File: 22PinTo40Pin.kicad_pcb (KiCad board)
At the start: 2 copper layers, 92 x 15 mm, 3 parts, among them J1 Conn_01x15, J2 Conn_01x22

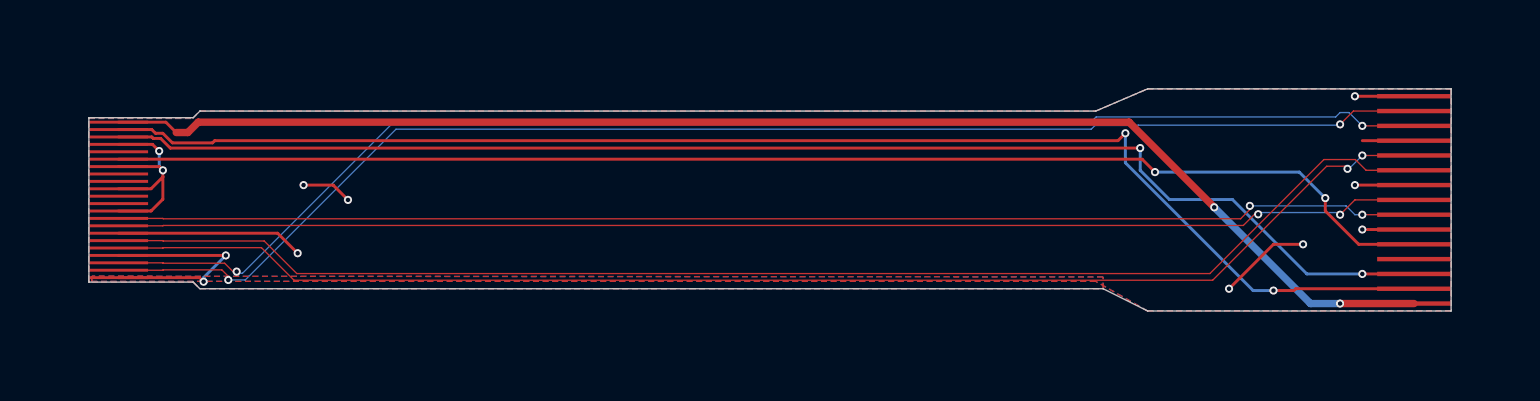
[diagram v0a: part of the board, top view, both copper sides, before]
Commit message: fixed lengths, fixed difference between pairs, actually corrected the pinout with 67% confidence of it working ok(hopium)
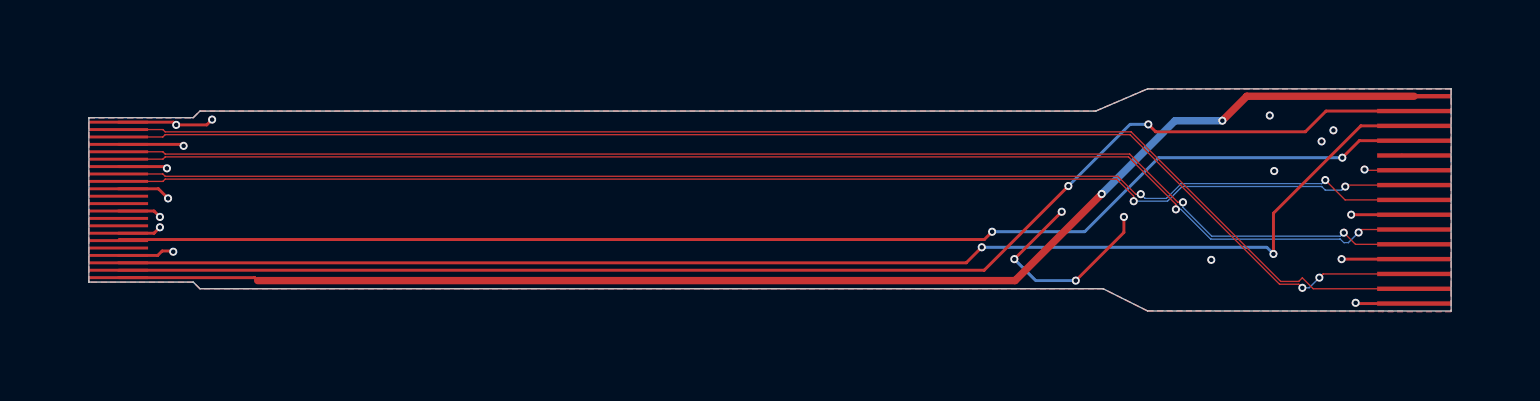
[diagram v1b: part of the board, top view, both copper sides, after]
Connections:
- J1 pad 1: GND -> +3.3V
- J1 pad 10: GND -> /CSI_D1_P
- J1 pad 11: Net-(J1-Pin_11) -> /CSI_D1_N
- J1 pad 12: unconnected-(J1-Pin_12-Pad12) -> GND
- J1 pad 13: Net-(J1-Pin_13) -> /CSI_D0_P
- J1 pad 14: Net-(J1-Pin_14) -> /CSI_D0_N
- J1 pad 15: +3.3V -> GND
- J1 pad 2: /CSI_D0_N -> Net-(J1-Pin_2)
- J1 pad 3: /CSI_D0_P -> Net-(J1-Pin_3)
- J1 pad 4: GND -> Net-(J1-Pin_4)
- J1 pad 5: /CSI_D1_N -> unconnected-(J1-Pin_5-Pad5)
- J1 pad 6: /CSI_D1_P -> GND
- J1 pad 7: GND -> /CSI_CLK_P
- J1 pad 9: /CSI_CLK_P -> GND
- J2 pad 1: GND -> +3.3V
- J2 pad 14: unconnected-(J2-Pin_14-Pad14) -> /CSI_CLK_P
- J2 pad 15: unconnected-(J2-Pin_15-Pad15) -> /CSI_CLK_N
- J2 pad 17: Net-(J1-Pin_11) -> /CSI_D1_P
- J2 pad 18: unconnected-(J2-Pin_18-Pad18) -> /CSI_D1_N
- J2 pad 2: /CSI_D0_N -> Net-(J1-Pin_2)
- J2 pad 20: Net-(J1-Pin_13) -> /CSI_D0_P
- J2 pad 21: Net-(J1-Pin_14) -> /CSI_D0_N
- J2 pad 22: +3.3V -> GND
- J2 pad 3: /CSI_D0_P -> Net-(J1-Pin_3)
- J2 pad 5: /CSI_D1_N -> unconnected-(J2-Pin_5-Pad5)
- J2 pad 6: /CSI_D1_P -> Net-(J1-Pin_4)
- J2 pad 8: /CSI_CLK_N -> unconnected-(J2-Pin_8-Pad8)
- J2 pad 9: /CSI_CLK_P -> unconnected-(J2-Pin_9-Pad9)
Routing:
- net Net-(J1-Pin_14): track 93.8 -> 0.00 mm, vias 2 -> 0
- net Net-(J1-Pin_3): track 0.00 -> 93.3 mm, vias 0 -> 2
- net Net-(J1-Pin_2): track 0.00 -> 92.4 mm, vias 0 -> 2
- net Net-(J1-Pin_13): track 92.2 -> 0.00 mm, vias 2 -> 0
- net Net-(J1-Pin_11): track 90.4 -> 0.00 mm, vias 2 -> 0
- net Net-(J1-Pin_4): track 0.00 -> 90.3 mm, vias 0 -> 2
- net GND: track 69.1 -> 59.2 mm, vias 12 -> 21
- net /CSI_D1_N: track 92.1 -> 90.5 mm
- net /CSI_D1_P: track 91.9 -> 90.5 mm, vias 0 -> 2
- net /CSI_CLK_N: track 88.3 -> 89.2 mm
- net unconnected-(J1-Pin_5-Pad5): track 0.00 -> 0.87 mm
- net /CSI_CLK_P: track 88.3 -> 89.0 mm
- net /CSI_D0_N: track 92.7 -> 92.2 mm, vias 2 -> 0

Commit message: forgot to ctrl-s on the last one lol
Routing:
- net /CSI_CLK_P: track 89.0 -> 92.5 mm
- net /CSI_CLK_N: track 89.2 -> 92.5 mm
- net /CSI_D0_N: track 92.2 -> 95.3 mm
- net /CSI_D1_P: track 90.5 -> 92.0 mm
- net /CSI_D1_N: track 90.5 -> 91.9 mm
